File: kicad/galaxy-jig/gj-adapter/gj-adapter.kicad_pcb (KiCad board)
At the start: 2 copper layers, 21 x 26.5 mm, 7 parts, among them J1 Conn_01x05, J2 Conn_01x04, J3 USB_B_Micro, U1 ADG723, U2 ADG723, U3 ADG723

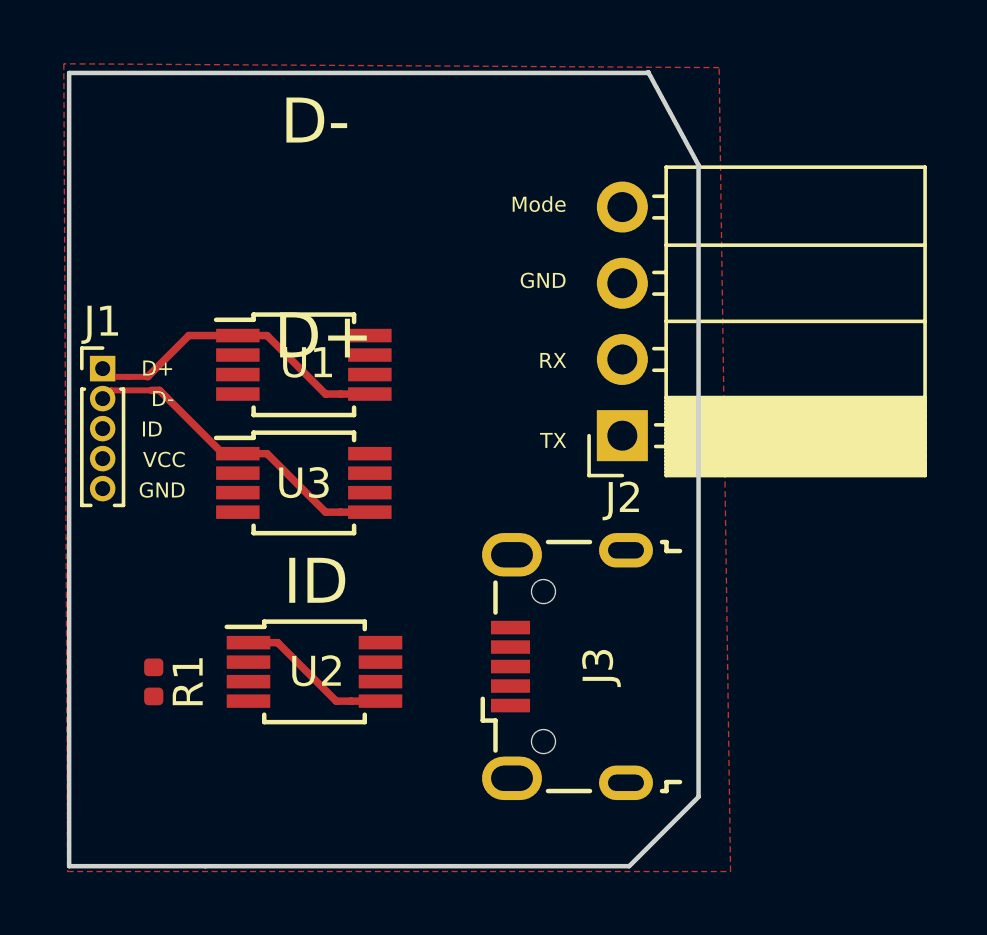
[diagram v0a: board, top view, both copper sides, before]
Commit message: kicad: semi-final version of galaxy-jig.
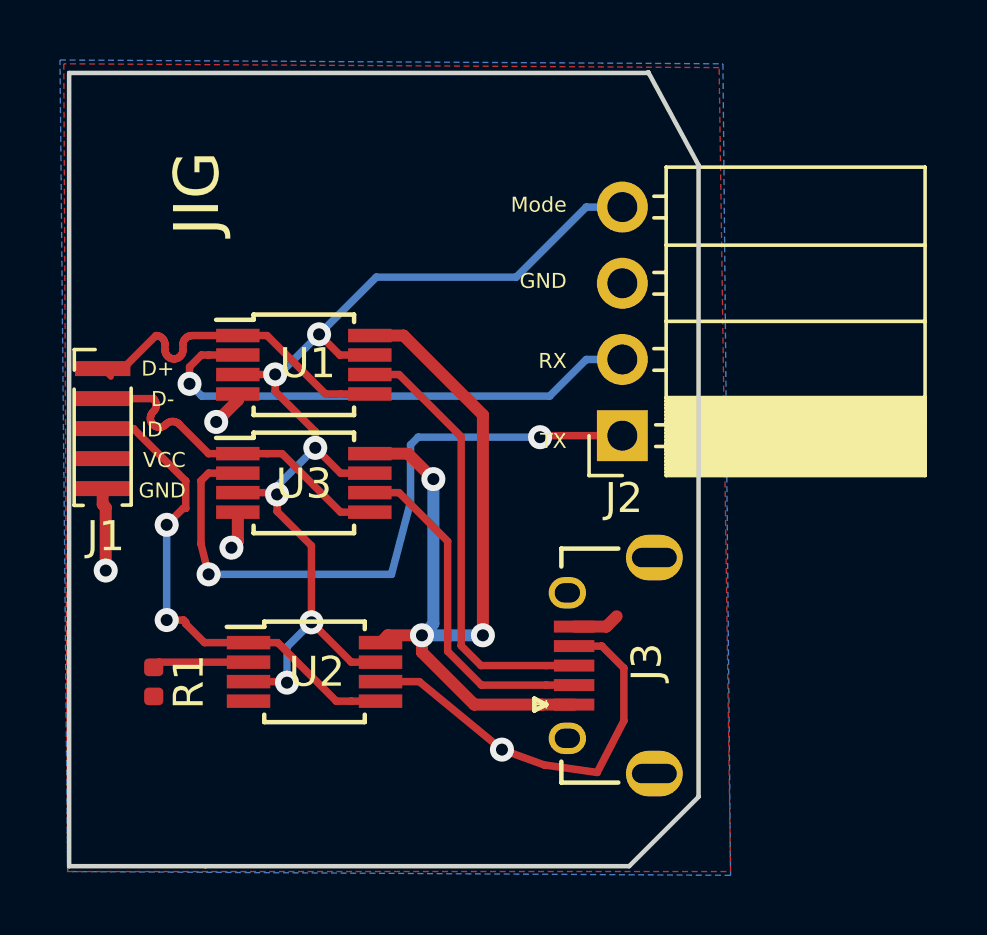
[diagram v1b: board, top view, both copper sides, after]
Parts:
- J3: footprint Connector_USB:USB_Micro-B_Wuerth_629105150521 -> Hirose:ZX62D-B-5PA8
- moved J3 2.90 mm to (136.8, 83.7)
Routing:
- net Mode: track 0.00 -> 36.9 mm, vias 0 -> 6
- net VCC: track 0.00 -> 29.9 mm, vias 0 -> 3
- net TX: track 0.00 -> 22.2 mm, vias 0 -> 2
- net RX: track 0.00 -> 17.4 mm, vias 0 -> 1
- net D+-PC: track 0.00 -> 14.9 mm
- net ID-PC: track 0.00 -> 13.8 mm, vias 0 -> 1
- net ID-device: track 5.21 -> 16.8 mm, vias 0 -> 2
- net D--PC: track 0.00 -> 11.6 mm
- net GND: track 0.00 -> 6.84 mm, vias 0 -> 3
- net Net-(R1-Pad1): track 0.00 -> 3.23 mm
- net D+: track 10.4 -> 11.6 mm
- added copper zone on B.Cu, net GND
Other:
- net class power: trace_width 0.5 -> 0.4
- board text added: "Galaxy"
- board text added: "JIG"
- board text added: "UART"
- board text added: "USB"
